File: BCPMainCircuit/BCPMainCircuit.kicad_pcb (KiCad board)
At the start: 2 copper layers, 94 x 88 mm, 52 parts, among them J1 MSD-4-A, Q1 IRLB8721PBF, SW1 Switch, U1 MCP9601T-E/MX, U2 Pico 2, U3 NEO-M9N-00B, U4 ICM-20948, U5 BME280, U9 AP63203WU-7

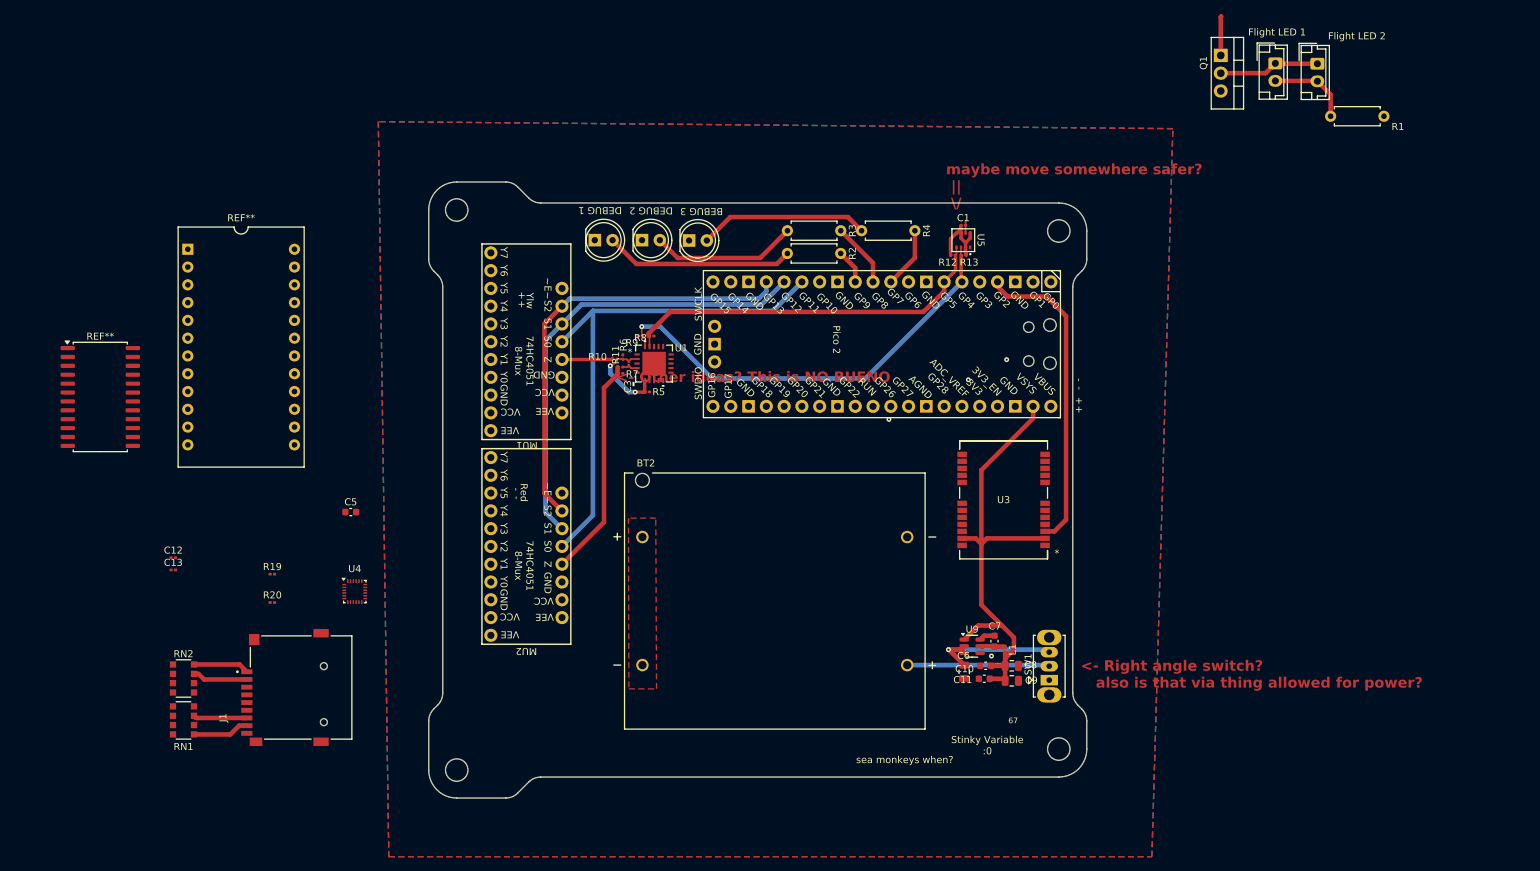
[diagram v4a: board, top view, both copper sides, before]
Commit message: finished magnetometer and imu still need: GPS stuff SD card stuff RGB LEDs
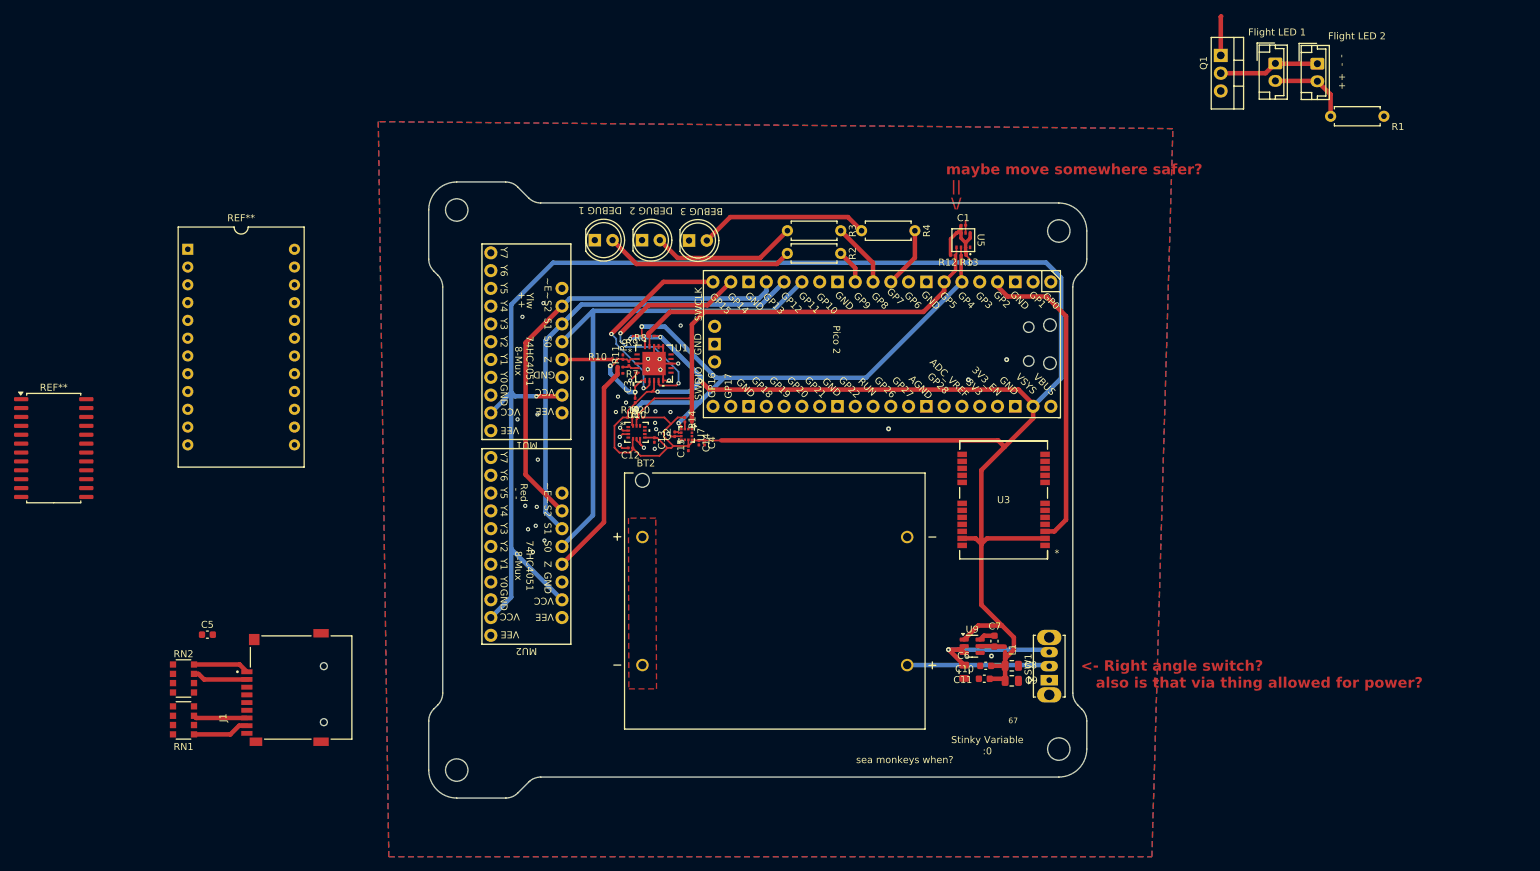
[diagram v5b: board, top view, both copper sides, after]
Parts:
- removed U4: ICM-20948, Sensor_Motion:InvenSense_QFN-24_3x3mm_P0.4mm
- added C14: 100nf, Capacitor_SMD:C_0201_0603Metric, F.Cu at (95.8, 93.1)
- added C15: 100nf, Capacitor_SMD:C_0201_0603Metric, F.Cu at (94.3, 93.9)
- added C2: 220nf, Capacitor_SMD:C_0201_0603Metric, F.Cu at (92.3, 91.9)
- added C4: 10uf, Capacitor_SMD:C_0201_0603Metric, F.Cu at (96.5, 93.1)
- added R14: 10kΩ, Resistor_SMD:R_0201_0603Metric, F.Cu at (93.8, 89.8)
- added U10: LSM6DSO, Gabriel_footprints:LSM6DSO, F.Cu at (86.8, 91.6)
- added U7: LIS2MDL, Package_LGA:LGA-12_2x2mm_P0.5mm, F.Cu at (94.0, 91.9)
- moved C13 71.2 mm to (89.4, 92.7), turned to -90 degrees
- moved C12 67.2 mm to (86.0, 93.8), turned to 180 degrees
- moved R20 58.9 mm to (87.4, 89.5)
- moved R19 55.8 mm to (85.9, 89.5)
- moved C5 26.9 mm to (25.6, 120.5)
- moved REF** 9.87 mm to (3.60, 93.8)
- moved R5 2.11 mm to (86.7, 87.1), turned to -90 degrees
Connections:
- BT2 pad N1: GND -> (no net)
- BT2 pad N2: BatTerms -> (no net)
- BT2 pad P1: BatTerms -> (no net)
- BT2 pad P2: Net-(BT2-+) -> (no net)
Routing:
- net +3.3V: track 79.1 -> 410.7 mm, vias 0 -> 6
- net /ThermoOCwarn: track 0.00 -> 35.3 mm, vias 0 -> 2
- net /ThermoSCwarn: track 0.00 -> 29.0 mm, vias 0 -> 2
- net /SCL: track 53.6 -> 81.6 mm
- net GND: track 1.78 -> 28.5 mm, vias 4 -> 37
- net /SDA: track 62.5 -> 84.7 mm, vias 1 -> 3
- net /TC-Sel3: track 62.7 -> 64.9 mm
- net Net-(U7-~{CS}): track 0.00 -> 1.02 mm
- net Net-(U7-C1): track 0.00 -> 0.98 mm
- added copper zone on F.Cu, net (none)
- removed copper zone on F.Cu, net BatTerms

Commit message: Replaced mux with different, smaller, smd, cheaper one put flight leds back
NEED TO DO:
add gps antenna
check if gps needs filter caps
verify v. reg capacitors (size, footprint, values)
figure out how sd cards work (im confused by them, for i have a simple mind)
breakout pins for everything we'd want
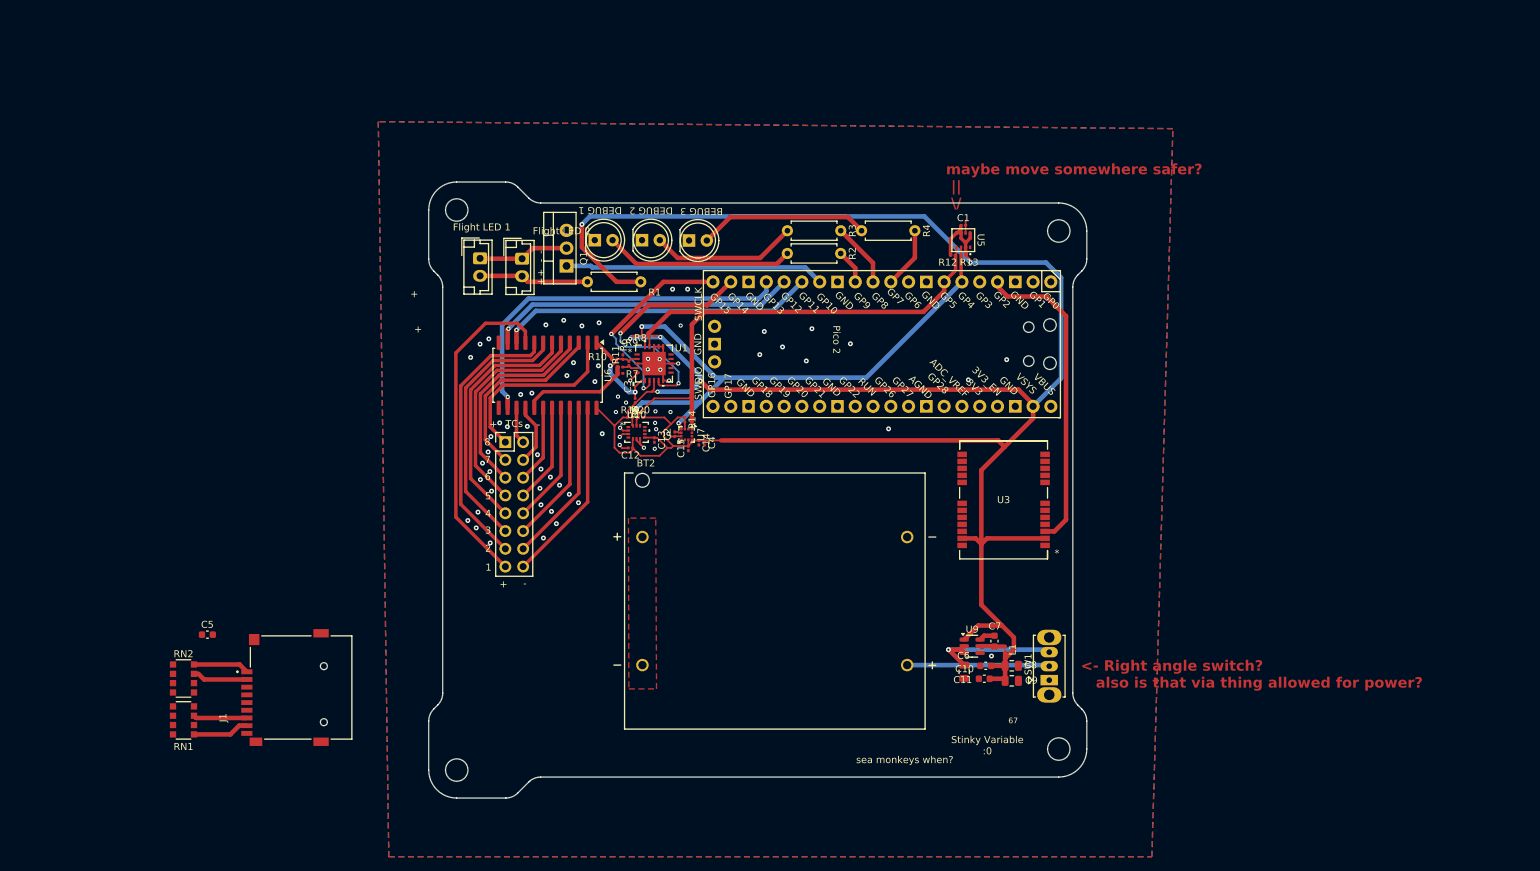
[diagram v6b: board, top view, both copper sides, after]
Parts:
- removed MU1, MU2: ~, Gabriel_footprints:74HC4051 8_1
- removed the REF** at (22.8, 65.5)
- removed the REF** at (3.60, 93.8)
- added TCs: PinHeader_2x08_P2.54mm_Vertical, Connector_PinHeader_2.54mm:PinHeader_2x08_P2.54mm_Vertical, F.Cu at (68.1, 93.0)
- added U6: CD4097B, Package_SO:SOIC-24W_7.5x15.4mm_P1.27mm, F.Cu at (74.2, 83.5)
- moved D1 117.0 mm to (64.5, 66.7)
- moved D5 117.0 mm to (70.5, 66.8)
- moved R1 108.8 mm to (87.5, 70.1)
- moved Q1 98.2 mm to (76.8, 67.8), turned to 90 degrees
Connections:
- U2 pad 14: unconnected-(U2-GPIO10-Pad14) -> /FLIGHTLED
- U2 pad 29: /FLIGHTLED -> unconnected-(U2-GPIO22-Pad29)
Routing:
- net +3.3V: track 410.7 -> 350.8 mm
- net /TC+1: track 0.00 -> 47.2 mm
- net /TC+2: track 0.00 -> 39.7 mm
- net /TC+3: track 0.00 -> 37.1 mm
- net /TC+4: track 0.00 -> 35.0 mm
- net /TC+5: track 0.00 -> 32.4 mm
- net /FLIGHTLED: track 5.62 -> 37.1 mm
- net /TC+6: track 0.00 -> 29.8 mm
- net /TC-Sel1: track 73.4 -> 45.4 mm, vias 0 -> 1
- net /TC+7: track 0.00 -> 27.2 mm
- net /TC+8: track 0.00 -> 26.8 mm
- net /TC-1: track 0.00 -> 26.5 mm
- net /TC-2: track 0.00 -> 23.4 mm
- net /TC-Sel2: track 65.4 -> 44.2 mm, vias 0 -> 1
- net /TC-3: track 0.00 -> 20.4 mm
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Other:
- board text added: "1"
- board text added: "2"
- board text added: "3"
- board text added: "4"
- board text added: "5"
- board text added: "6"
- board text added: "7"
- board text added: "8"
- board text removed: "Red"
- board text removed: "Ylw"
